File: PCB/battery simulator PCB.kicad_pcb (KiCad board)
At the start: 4 copper layers, 52.5 x 50 mm, 22 parts, among them U1 OPA569DWP

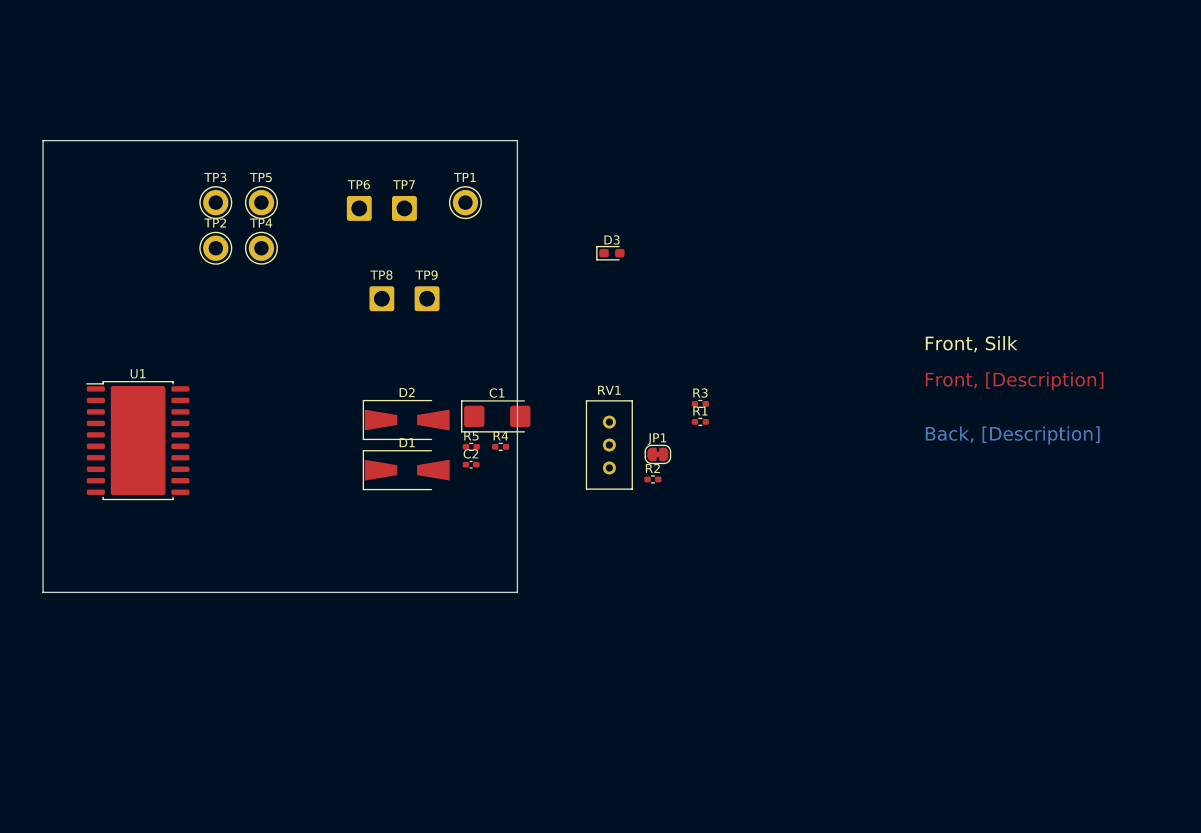
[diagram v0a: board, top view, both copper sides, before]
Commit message: Added FUSB302B and associated circuitry.
Added FUSB302B, along with USB-C Connector and LDO.  The LDO is
needed to power the FUSB302B from the cable.

Also added some debugging and convenience items such as a QWIIC
connector and some test points.
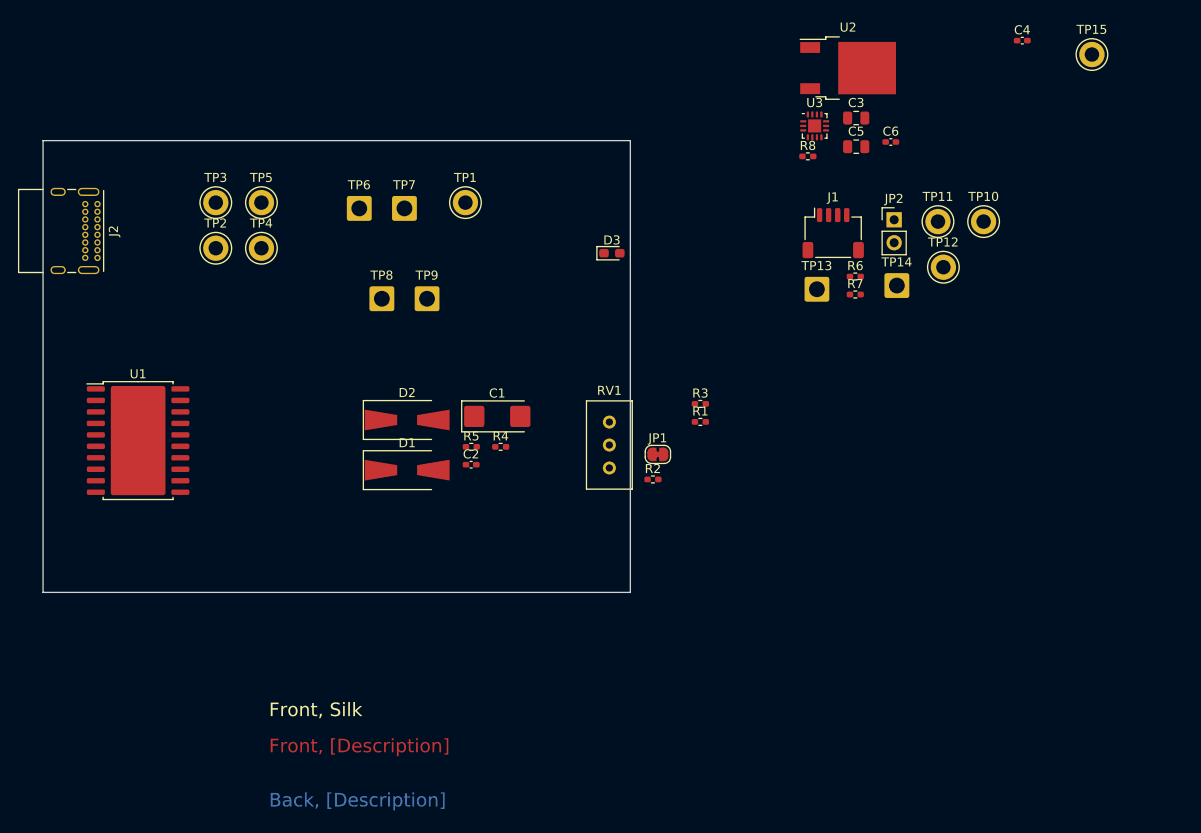
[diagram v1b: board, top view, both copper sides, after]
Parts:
- added C3: 2.2u, Capacitor_SMD:C_0805_2012Metric, F.Cu at (140.0, 47.5)
- added C4: 0.1u, Capacitor_SMD:C_0402_1005Metric_Pad0.74x0.62mm_HandSolder, F.Cu at (158.4, 38.9)
- added C5: 2.2u, Capacitor_SMD:C_0805_2012Metric, F.Cu at (140.0, 50.7)
- added C6: 0.1u, Capacitor_SMD:C_0402_1005Metric_Pad0.74x0.62mm_HandSolder, F.Cu at (143.8, 50.1)
- added J1: QWIIC, Connector_JST:JST_SH_SM04B-SRSS-TB_1x04-1MP_P1.00mm_Horizontal, F.Cu at (137.4, 60.2)
- added J2: USB_C_Receptacle_USB2.0, Connector_USB:USB_C_Receptacle_GCT_USB4085, F.Cu at (56.0, 57.0)
- added JP2: Jumper_2_Open, Connector_PinHeader_2.54mm:PinHeader_1x02_P2.54mm_Vertical, F.Cu at (144.2, 58.8)
- added R6: 2.2k, Resistor_SMD:R_0402_1005Metric_Pad0.72x0.64mm_HandSolder, F.Cu at (139.9, 65.0)
- added R7: 2.2k, Resistor_SMD:R_0402_1005Metric_Pad0.72x0.64mm_HandSolder, F.Cu at (139.9, 67.0)
- added R8: 4.7k, Resistor_SMD:R_0402_1005Metric_Pad0.72x0.64mm_HandSolder, F.Cu at (134.7, 51.7)
- added TP10: TestPoint, TestPoint:TestPoint_Keystone_5010-5014_Multipurpose, F.Cu at (154.1, 59.0)
- added TP11: TestPoint, TestPoint:TestPoint_Keystone_5010-5014_Multipurpose, F.Cu at (149.1, 59.0)
- added TP12: TestPoint, TestPoint:TestPoint_Keystone_5010-5014_Multipurpose, F.Cu at (149.7, 64.0)
- added TP13: TestPoint, Connector_Wire:SolderWire-1sqmm_1x01_D1.4mm_OD2.7mm, F.Cu at (135.7, 66.5)
- added TP14: TestPoint, Connector_Wire:SolderWire-1sqmm_1x01_D1.4mm_OD2.7mm, F.Cu at (144.5, 66.0)
- added TP15: TestPoint, TestPoint:TestPoint_Keystone_5010-5014_Multipurpose, F.Cu at (166.1, 40.5)
- added U2: BD33C0AFP-CE2, Package_TO_SOT_SMD:TO-252-2, F.Cu at (139.1, 42.0)
- added U3: FUSB302BMPX, Package_DFN_QFN:WQFN-14-1EP_2.5x2.5mm_P0.5mm_EP1.45x1.45mm, F.Cu at (135.4, 48.4)
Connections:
- C1 pad 1: +5V -> VBUS
- C2 pad 2: +5V -> VBUS
- D2 pad 1: +5V -> VBUS
- D3 pad 2: +5V -> +3.3V
- R1 pad 1: +5V -> VBUS
- TP8 pad 1: +5V -> VBUS
- U1 pad 12: +5V -> VBUS
- U1 pad 13: +5V -> VBUS
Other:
- board size 52.5 x 50 mm -> 65 x 50 mm

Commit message: Imported and placed all components into PCB.
Imported all components into PCB.  Finalized PCB outline to 50mm x
50mm square.  Arranged all components into reasonable locations
and added 2 planes.

Schematic update is just adding netlabels to the CC1 and CC2 nets.
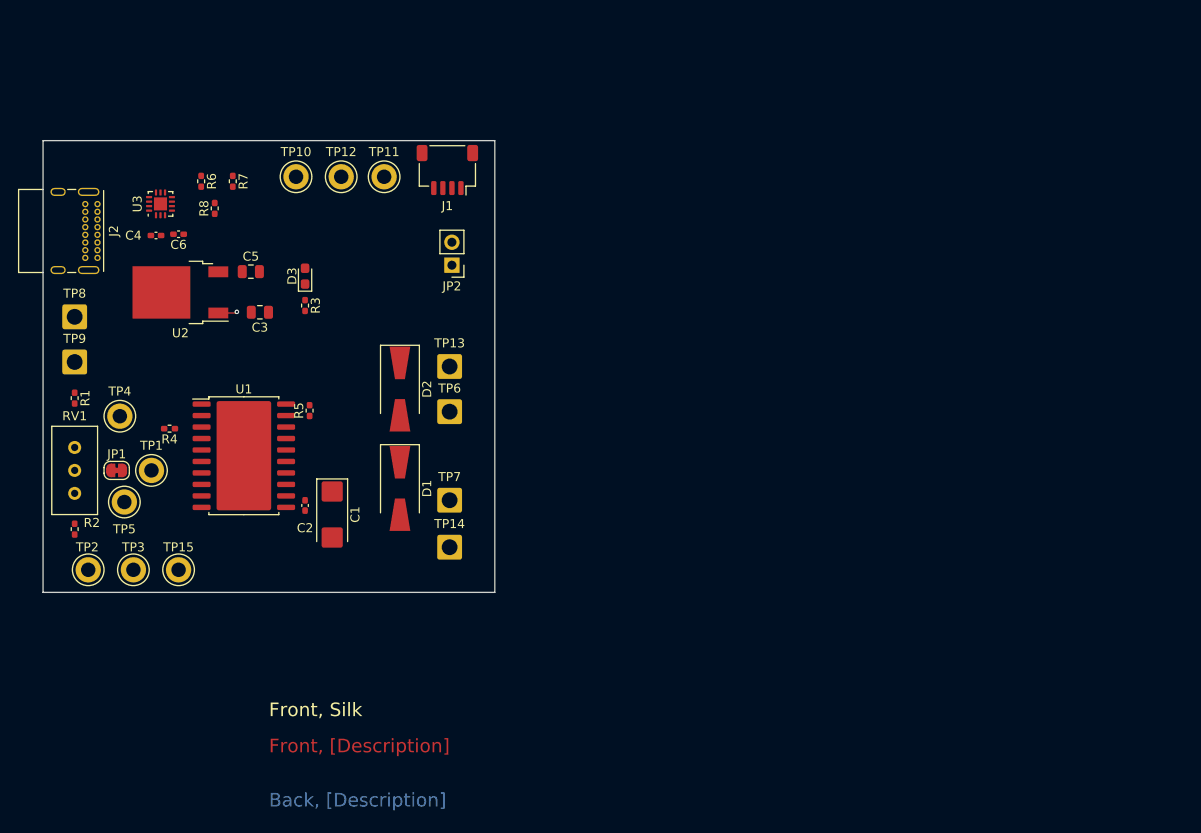
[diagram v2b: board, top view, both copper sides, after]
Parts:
- moved TP15 116.1 mm to (65.0, 97.5)
- moved C4 98.3 mm to (62.5, 60.5)
- moved C6 79.5 mm to (65.0, 60.4), turned to 180 degrees
- moved U2 78.0 mm to (65.2, 66.8), turned to 180 degrees
- moved TP10 76.3 mm to (78.0, 54.0)
- moved R6 73.2 mm to (67.5, 54.5), turned to -90 degrees
- moved U3 72.9 mm to (63.0, 57.0), turned to 90 degrees
- moved R7 70.0 mm to (71.0, 54.5), turned to -90 degrees
- moved C3 69.4 mm to (74.0, 69.0), turned to 180 degrees
- moved R1 69.3 mm to (53.5, 78.5), turned to -90 degrees
- moved C5 68.4 mm to (73.0, 64.5)
- moved TP12 67.4 mm to (83.0, 54.0)
- moved R8 65.9 mm to (69.0, 57.5), turned to 90 degrees
- moved R2 64.2 mm to (53.5, 93.0), turned to -90 degrees
- moved TP11 61.5 mm to (87.8, 54.0)
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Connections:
- net Net-(J2-PadA5) renamed /Power Input/CC1
- net Net-(J2-PadB5) renamed /Power Input/CC2
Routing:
- net VBUS: track 0.00 -> 2.10 mm, vias 0 -> 1
- added copper zone on In2.Cu, net GND
- added copper zone on In1.Cu, net VBUS
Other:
- board size 65 x 50 mm -> 50 x 50 mm

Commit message: Update to KiCAD v7, and finalize for V1 build
Updated to KiCAD v7, which touched many files.

Also made some changes to finalize board for prototype build.  Simplified the
circuit a bit to just something built and tested.
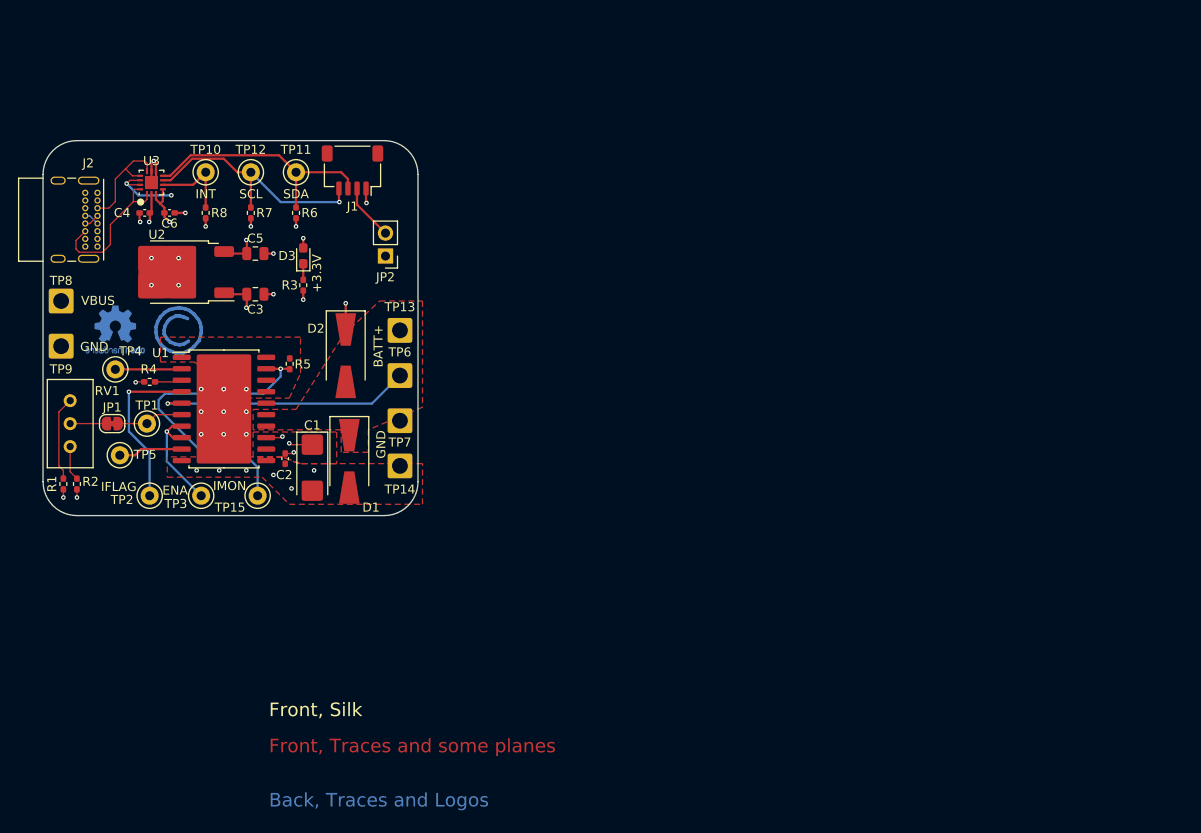
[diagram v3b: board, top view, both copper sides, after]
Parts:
- added REF**: KiCad-Logo2_6mm_SilkScreen, Symbol:KiCad-Logo2_6mm_SilkScreen, B.Cu at (77.1, 62.0)
- added REF**: Symbol_CC-ShareAlike_CopperTop_Small, Symbol:Symbol_CC-ShareAlike_CopperTop_Small, B.Cu at (65.0, 71.0)
- added REF**: OSHW-Logo2_7.3x6mm_Copper, Symbol:OSHW-Logo2_7.3x6mm_Copper, B.Cu at (58.0, 71.0)
- RV1: footprint Potentiometer_THT:Potentiometer_Bourns_3386C_Horizontal -> Potentiometer_THT:Potentiometer_Bourns_3296W_Vertical
- TP1, TP10, TP11, TP12, TP15, TP4, TP5: footprint TestPoint:TestPoint_Keystone_5010-5014_Multipurpose -> TestPoint:TestPoint_Keystone_5000-5004_Miniature
- TP2, TP3: footprint TestPoint:TestPoint_Keystone_5005-5009_Compact -> TestPoint:TestPoint_Keystone_5000-5004_Miniature
- moved TP15 12.0 mm to (73.8, 89.3)
- moved TP3 11.1 mm to (67.5, 89.3)
- moved R6 11.1 mm to (78.0, 58.0), turned to 90 degrees
- moved TP2 10.7 mm to (61.8, 89.3)
- moved TP14 10.5 mm to (89.5, 86.0)
- moved J1 10.5 mm to (84.2, 53.3)
- moved TP7 10.4 mm to (89.5, 81.0)
- moved TP10 10.0 mm to (68.0, 53.5)
- moved TP12 10.0 mm to (73.0, 53.5)
- moved TP11 9.76 mm to (78.0, 53.5)
- moved R1 9.58 mm to (52.2, 88.0), turned to 90 degrees
- moved JP2 7.42 mm to (87.9, 62.8)
- moved D2 7.05 mm to (83.5, 73.8)
- moved TP13 6.80 mm to (89.5, 71.0)
- moved TP6 6.80 mm to (89.5, 76.0)
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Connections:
- J2 pad A6: unconnected-(J2-PadA6) -> Net-(J2-D+-PadA6)
- J2 pad A7: unconnected-(J2-PadA7) -> Net-(J2-D--PadA7)
- J2 pad B6: unconnected-(J2-PadB6) -> Net-(J2-D+-PadA6)
- J2 pad B7: unconnected-(J2-PadB7) -> Net-(J2-D--PadA7)
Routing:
- net Net-(U1-IMON): track 0.00 -> 35.8 mm, vias 0 -> 1
- net /Power Regulation/Power Out: track 0.00 -> 28.6 mm, vias 0 -> 1
- net /SCL: track 0.00 -> 27.9 mm, vias 0 -> 1
- net /SDA: track 0.00 -> 27.5 mm
- net +3.3V: track 0.00 -> 22.0 mm, vias 0 -> 8
- net Net-(U1-~{IFLAG}): track 0.00 -> 18.3 mm, vias 0 -> 1
- net /Power Input/CC2: track 0.00 -> 16.7 mm
- net VBUS: track 2.10 -> 16.6 mm, vias 1 -> 7
- net GND: track 0.00 -> 14.0 mm, vias 0 -> 28
- net Net-(U1-ENA): track 0.00 -> 12.5 mm, vias 0 -> 1
- net /Power Input/CC1: track 0.00 -> 12.0 mm
- net Net-(R1-Pad2): track 0.00 -> 9.35 mm
- net /Power Input/INT: track 0.00 -> 9.22 mm
- net /Power Regulation/Setting IN: track 0.00 -> 7.46 mm
- net Net-(U1-POUT1): track 0.00 -> 7.38 mm
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- added copper zone on In1.Cu, net +3.3V
- added copper zone on F.Cu, net /Power Regulation/Power Out
- added copper zone on F.Cu, net GND
- added copper zone on F.Cu, net VBUS
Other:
- board size 50 x 50 mm -> 41.5 x 41.5 mm
- board text added: "+3.3V"
- board text added: "BATT+"
- board text added: "Back, Traces and Logos"
- board text added: "ENA"
- board text added: "Front, Traces and some planes"
- board text added: "GND"
- board text added: "IFLAG"
- board text added: "IMON"
- board text added: "INT"
- board text added: "In1, Power planes, VBUS and 3.3V"
- board text added: "In2, Ground Plane"
- board text added: "SCL"
- board text added: "SDA"
- board text added: "SK Electronics Battery Simulator V1 2023 May 12"
- board text added: "VBUS"
- board text removed: "Back, [Description]"
- board text removed: "Front, [Description]"
- board text removed: "In1, [Description]"
- board text removed: "In2, [Description]"
